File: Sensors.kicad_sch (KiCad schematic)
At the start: 7 parts, among them M13 Module-knock-0.2, M5 Module-vr-discrete-0.5, M7 Module-knock-0.2

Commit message: EmbeddedEra libraries and template, KiCad 10
- Every symbol except the nine Hellen-One modules now comes from the EmbeddedEra library (resistors and 0R links from the generic libraries, PTC fuses, VND14NV04-E, TE 1-1376430-0, Molex 39281143, test pads, proto area, power symbols). Same-pin parts swapped in place; resistors re-placed between their old pin points with short wires. New parts live on library branch sti2004-parts.
- EmbeddedEra project template: worksheet, text variables, net classes with explicit power classes, JLCPCB design rules; template net names for USB, I2C and the K-line UART.
- Migrated all sheets and the board to KiCad 10 (10.0.7).
- tools/sch_overlap_check.py also fails on overlapping symbol bodies and on fields printed across a wire (found the stacked PTC fuses); KiCad 10 hide flags understood.

Verified: connectivity identical to the previous commit (167 nets), only the planned net renames; 0 overlaps on all 10 sheet files; ERC errors unchanged (148); pinout check 99 OK.

Co-Authored-By: Claude Opus 5.5 <noreply@anthropic.com>
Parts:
- removed JP8: 0R, hellen-one-common:PAD-0805-PAD, symbol hellen-one-common:Jumper-Pad-Pad
- removed JP9: DNP 0R, hellen-one-common:PAD-0805-PAD, symbol hellen-one-common:Jumper-Pad-Pad
- removed R42, R43: 1k, hellen-one-common:R0603, symbol hellen-one-common:Res
- added JP8, JP9: 0, EmbeddedEra_Library:R_0805_2012Metric, symbol EmbeddedEra_Resistors_0805_5pct:EE_R_0805_0_5%
- added R42, R43: 1K, EmbeddedEra_Library:R_0603_1608Metric, symbol EmbeddedEra_Resistors_0603:EE_R_0603_1K_1%
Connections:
- net +5VA: now also R42.2, R43.2
- net GND: now also JP8.2
- net GNDA: now also JP9.2
- net GND_SENSOR: now also JP8.1, JP9.1
- net IN_CAM: now also R42.1
- net IN_CAM_RH: now also R43.1

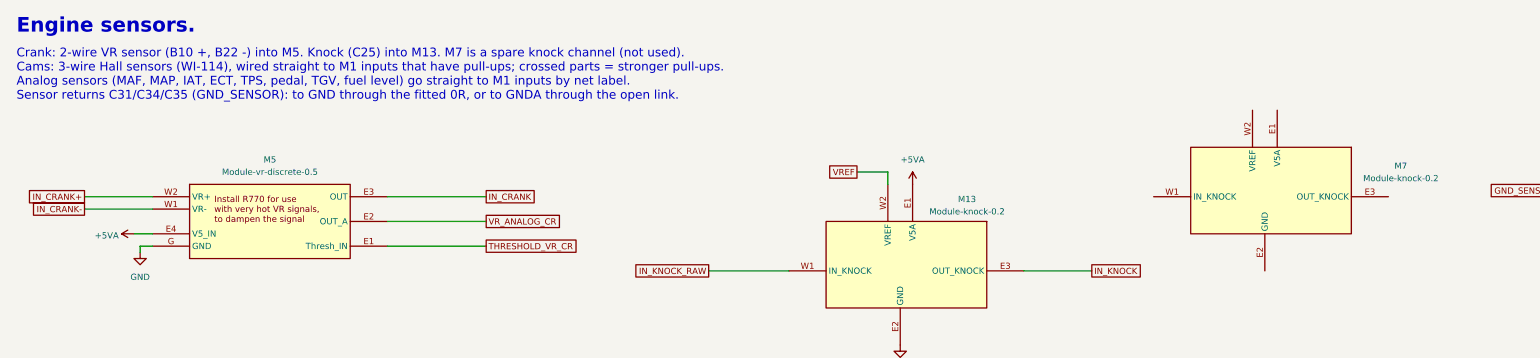
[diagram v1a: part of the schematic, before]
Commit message: Remove unused M7 knock module and a stray plug note; checker models KiCad's field-justify flip
- M7 (second knock module) had no pin connected; the STI has one knock sensor (C25) on M13.
- 'D: B137' free text (rev-a leftover) duplicated J1's own plug label and sat on the Aux sheet.
- sch_overlap_check: KiCad draws a field's left/right justification mirrored for some
  angle/rotation/mirror combinations (measured from kicad-cli 10 PDF output); the checker now
  boxes those fields where KiCad draws them.

Co-Authored-By: Claude Opus 5.5 <noreply@anthropic.com>
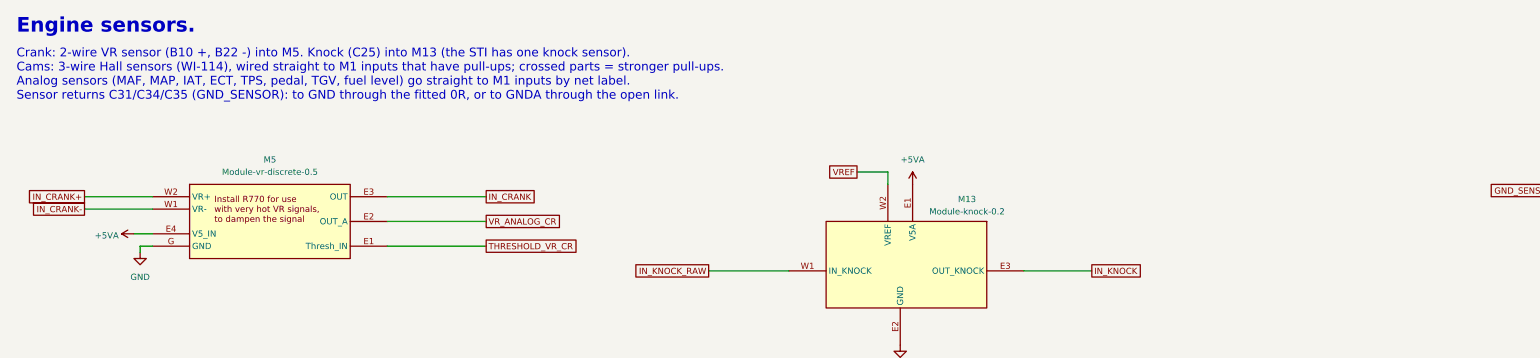
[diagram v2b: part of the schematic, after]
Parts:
- removed M7: Module-knock-0.2, hellen-one-knock-0.2:knock, symbol hellen-one-knock-0.2:Module-knock-0.2
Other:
- note added: "Crank: 2-wire VR sensor (B10 +, B22 -) into M5. Knock (C25) into M13 (the STI has one knock sensor). Cams: 3-wire Hall sensors (WI-114), wired straight to M1 inputs that have pull-ups; crossed parts = stronger pull-ups. Analog sensors (MAF, MAP, IAT, ECT, TPS, pedal, TGV, fuel level) go straight to M1 inputs by net label. Sensor returns C31/C34/C35 (GND_SENSOR): to GND through the fitted 0R, or t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"
- note removed: "Crank: 2-wire VR sensor (B10 +, B22 -) into M5. Knock (C25) into M13. M7 is a spare knock channel (not used). Cams: 3-wire Hall sensors (WI-114), wired straight to M1 inputs that have pull-ups; crossed parts = stronger pull-ups. Analog sensors (MAF, MAP, IAT, ECT, TPS, pedal, TGV, fuel level) go straight to M1 inputs by net label. Sensor returns C31/C34/C35 (GND_SENSOR): to GND through the fitted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"
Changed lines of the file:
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@@
 		)
 	)
-	(text "Crank: 2-wire VR sensor (B10 +, B22 -) into M5. Knock (C25) into M13. M7 is a spare knock channel (not used).\nCams: 3-wire Hall sensors (WI-114), wired straight to M1 inputs that have pull-ups; crossed parts = stronger pull-ups.\nAnalog sensors (MAF, MAP, IAT, ECT, TPS, pedal, TGV, fuel level) go straight to M1 inputs by net label.\nSensor returns C31/C34/C35 (GND_SENSOR): to GND through the fitted 0R, or to GNDA through the open link."
+	(text "Crank: 2-wire VR sensor (B10 +, B22 -) into M5. Knock (C25) into M13 (the STI has one knock sensor).\nCams: 3-wire Hall sensors (WI-114), wired straight to M1 inputs that have pull-ups; crossed parts = stronger pull-ups.\nAnalog sensors (MAF, MAP, IAT, ECT, TPS, pedal, TGV, fuel level) go straight to M1 inputs by net label.\nSensor returns C31/C34/C35 (GND_SENSOR): to GND through the fitted 0R, or to GNDA through the open link."
 		(exclude_from_sim no)
 		(at 15.24 22.86 0)
@@
 					(unit 1)
 				)
-			)
-		)
-	)
-	(symbol
-		(lib_id "hellen-one-knock-0.2:Module-knock-0.2")
-		(at 256.54 43.18 0)
-		(unit 1)
-		(body_style 1)
-		(exclude_from_sim no)
-		(in_bom yes)
-		(on_board yes)
-		(in_pos_files yes)
-		(dnp no)
-		(fields_autoplaced yes)
-		(property "Reference" "M7"
-			(at 299.72 47.0214 0)
-			(show_name no)
-			(do_not_autoplace no)
-			(effects
-				(font
-					(size 1.27 1.27)
-				)
-			)
-		)
-		(property "Value" "Module-knock-0.2"
-			(at 299.72 49.5614 0)
-			(show_name no)
-			(do_not_autoplace no)
-			(effects
-				(font
-					(size 1.27 1.27)
-				)
-			)
-		)
-		(property "Footprint" "hellen-one-knock-0.2:knock"
-			(at 256.54 43.18 0)
-			(hide yes)
-			(show_name no)
-			(do_not_autoplace no)
-			(effects
-				(font
-					(size 1.27 1.27)
-				)
-			)
-		)
-		(property "Datasheet" ""
-			(at 256.54 43.18 0)
-			(hide yes)
-			(show_name no)
-			(do_not_autoplace no)
-			(effects
-				(font
-					(size 1.27 1.27)
-				)
-			)
-		)
-		(property "Description" "Hellen-One Knock Pre-amplifier Module"
-			(at 256.54 43.18 0)
-			(hide yes)
-			(show_name no)
-			(do_not_autoplace no)
-			(effects
-				(font
-					(size 1.27 1.27)
-				)
-			)
-		)
-		(pin "E2"
-		)
-		(pin "W2"
-		)
-		(pin "E1"
-		)
-		(pin "E3"
-		)
-		(pin "W1"
-		)
-		(instances
-			(project ""
-				(path "/00d4d98c-a749-4bd2-a087-ea484becbbe4/174c6130-5ef2-5679-8495-7e10ec78ddae"
-					(reference "M7")
-					(unit 1)
-				)
